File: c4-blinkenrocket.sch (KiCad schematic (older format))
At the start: 12 parts, among them J1 ISP, U1 ATtiny88-AU

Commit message: A first complete Version of the Blinkenrocket
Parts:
- added C3: 470 nF, Capacitor_SMD:C_1206_3216Metric_Pad1.42x1.75mm_HandSolder, symbol Device:C
- added H2, H3: MountingHole, MountingHole:MountingHole_3.2mm_M3_Pad, symbol Mechanical:MountingHole
- added JP1: SJ1-3523N, footprints:Jack_3.5mm_CUI_SJ1-3523N_Horizontal, symbol SJ1-3523N:SJ1-3523N
- added JP3, JP4: Conn_01x04, Connector_PinHeader_2.54mm:PinHeader_1x04_P2.54mm_Vertical, symbol Connector_Generic:Conn_01x04
- added LED1: LED_Matrix_8x8, footprints:LED_KWM-30881XVB_8x8_3mm_3.2x3.2mm, symbol LED_Matrix_8x8:LED_Matrix_8x8
- added R4, R5: 10k, Resistor_SMD:R_1206_3216Metric_Pad1.42x1.75mm_HandSolder, symbol Device:R
- added SW1, SW2: SW_SPST, Button_Switch_THT:SW_PUSH_6mm_H5mm, symbol Switch:SW_SPST
- added U2: 24CW640-I_SN, Package_SO:SOIC-8_3.9x4.9mm_P1.27mm, symbol 24CW640:24CW640-I_SN
- C1, C2: footprint Capacitor_SMD:C_1206_3216Metric -> Capacitor_SMD:C_1206_3216Metric_Pad1.42x1.75mm_HandSolder
- H1: renamed from H?; footprint MountingHole:MountingHole_3.2mm_M3 -> MountingHole:MountingHole_3.2mm_M3_Pad
- R1: footprint Resistor_SMD:R_1206_3216Metric -> Resistor_SMD:R_1206_3216Metric_Pad1.42x1.75mm_HandSolder
- R2: renamed from R3; footprint Resistor_SMD:R_1206_3216Metric -> Resistor_SMD:R_1206_3216Metric_Pad1.42x1.75mm_HandSolder
- R3: renamed from R2; footprint Resistor_SMD:R_1206_3216Metric -> Resistor_SMD:R_1206_3216Metric_Pad1.42x1.75mm_HandSolder
- R6: renamed from R4; footprint Resistor_SMD:R_1206_3216Metric -> Resistor_SMD:R_1206_3216Metric_Pad1.42x1.75mm_HandSolder
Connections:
- net GND: now also C3.1, JP1.1 (S), JP3.4 (Pin_4), JP4.4 (Pin_4), SW1.2 (B), SW2.2 (B), U2.4 (VSS)
- net MISO: now also LED1.1 (ROW5)
- net MOSI: now also LED1.12 (ROW4)
- net VCC: now also C3.2, JP3.1 (Pin_1), JP4.1 (Pin_1), R4.2, R5.2, U2.8 (VCC)
- net C4: now reaches U1.1 (PD3)
- net C4: now also LED1.10 (COL4)
- net C7: now reaches U1.10 (PD6)
- net C7: now also LED1.15 (COL7)
- net C8: now reaches U1.11 (PD7)
- net C8: now also LED1.16 (COL8)
- net R1: now reaches U1.12 (PB0)
- net R1: now also LED1.9 (ROW1)
- net R2: now reaches U1.13 (PB1)
- net R2: now also LED1.14 (ROW2)
- net R3: now reaches U1.14 (PB2)
- net R3: now also LED1.8 (ROW3)
- net C5: now reaches U1.2 (PD4)
- net C5: now also LED1.6 (COL5)
- net B1: now reaches U1.20 (PC7)
- net B1: now also SW1.1 (A)
- net E4: now reaches U1.22 (PA1)
- net E4: now also JP4.3 (Pin_3)
- net E1: now reaches U1.23 (PC0)
- net E1: now also JP3.2 (Pin_2)
- net E2: now reaches U1.24 (PC1)
- net E2: now also JP3.3 (Pin_3)
- net E3: now reaches U1.25 (PC2)
- net E3: now also JP4.2 (Pin_2)
- net B2: now reaches U1.26 (PC3)
- net B2: now also SW2.1 (A)
- net SDA: now reaches U1.27 (PC4)
- net SDA: now also R4.1, U2.5 (SDA)
- net SCL: now reaches U1.28 (PC5)
- net SCL: now also R5.1, U2.6 (SCL)
- net C1: now reaches U1.30 (PD0)
- net C1: now also LED1.13 (COL1)
- net C2: now reaches U1.31 (PD1)
- net C2: now also LED1.3 (COL2)
- net C3: now reaches U1.32 (PD2)
- net C3: now also LED1.4 (COL3)
- net R7: now reaches U1.7 (PB6)
- net R7: now also LED1.2 (ROW7)
- net R8: now reaches U1.8 (PB7)
- net R8: now also LED1.5 (ROW8)
- net C6: now reaches U1.9 (PD5)
- net C6: now also LED1.11 (COL6)
- net at R3.2: now also JP1.3 (R)
- net SCK renamed R6
- net R6: now also LED1.7 (ROW6)
- no-connect marks 0 -> 2
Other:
- moved on the sheet: C1, C2, D1, D2, H1, R1, R2, R3, U1

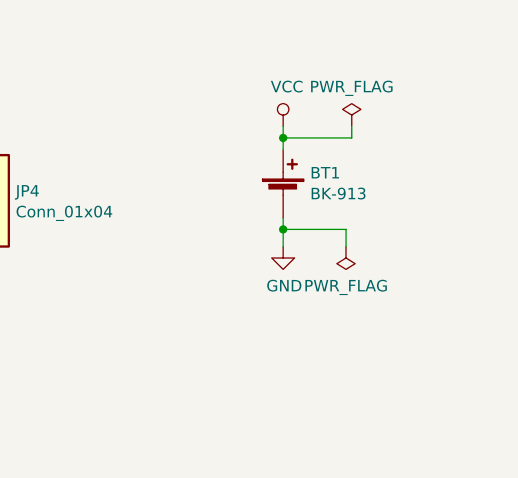
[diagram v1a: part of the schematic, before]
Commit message: Swapped battery holder, made footprints easier to solder
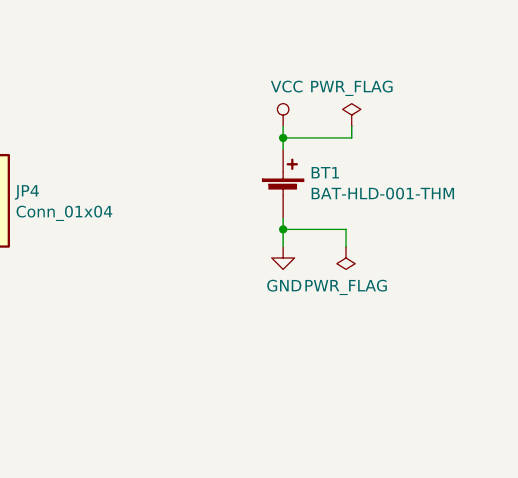
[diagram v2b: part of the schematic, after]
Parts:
- BT1: value BK-913 -> BAT-HLD-001-THM; footprint footprints:BAT_BK-913_footprint -> footprints:BAT_Linx_BAT-HLD-001-THM; Description Battery Retainer Coin, 20.0mm 1 Cell PC Pin -> BATTERY RETAINER COIN PC PIN; Digikey BK-913-ND -> BAT-HLD-001-THM-ND; Mfg Name MPD (Memory Protection Devices) -> Linx Technologies Inc.; Mfg Part Num BK-913 -> BAT-HLD-001-THM
- U1: footprint Package_QFP:TQFP-32_7x7mm_P0.8mm -> footprints:TQFP-32_7x7mm_P0.8mm_Handsolder; Description (none) -> IC MCU 8BIT 8KB FLASH 32TQFP; Digikey (none) -> ATTINY88-AU-ND; Mfg Name (none) -> Microchip Technology; Mfg Part Num (none) -> ATTINY88-AU
- U2: footprint Package_SO:SOIC-8_3.9x4.9mm_P1.27mm -> footprints:SOIC-8_4.9x3.9mm_P1.27mm_Handsolder
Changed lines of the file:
@@
 F 0 "U1" H 1675 1025 50  0000 R CNN
 F 1 "ATtiny88-AU" H 2675 4525 50  0000 R CNN
-F 2 "Package_QFP:TQFP-32_7x7mm_P0.8mm" H 2075 2775 50  0001 C CIN
+F 2 "footprints:TQFP-32_7x7mm_P0.8mm_Handsolder" H 2075 2775 50  0001 C CIN
 F 3 "http://ww1.microchip.com/downloads/en/DeviceDoc/doc8008.pdf" H 2075 2775 50  0001 C CNN
+F 4 "Microchip Technology" H 2075 2775 50  0001 C CNN "Mfg Name"
+F 5 "ATTINY88-AU" H 2075 2775 50  0001 C CNN "Mfg Part Num"
+F 6 "ATTINY88-AU-ND" H 2075 2775 50  0001 C CNN "Digikey"
+F 7 "IC MCU 8BIT 8KB FLASH 32TQFP" H 2075 2775 50  0001 C CNN "Description"
 	1    2075 2775
 	1    0    0    -1
@@
 P 10425 1425
 F 0 "BT1" H 10543 1521 50  0000 L CNN
-F 1 "BK-913" H 10543 1430 50  0000 L CNN
-F 2 "footprints:BAT_BK-913_footprint" V 10425 1485 50  0001 C CNN
-F 3 "http://www.memoryprotectiondevices.com/datasheets/BK-913-datasheet.pdf" V 10425 1485 50  0001 C CNN
-F 4 "MPD (Memory Protection Devices)" H 10425 1425 50  0001 C CNN "Mfg Name"
-F 5 "BK-913 " H 10425 1425 50  0001 C CNN "Mfg Part Num"
-F 6 "BK-913-ND" H 10425 1425 50  0001 C CNN "Digikey"
-F 7 "Battery Retainer Coin, 20.0mm 1 Cell PC Pin " H 10425 1425 50  0001 C CNN "Description"
+F 1 "BAT-HLD-001-THM" H 10543 1430 50  0000 L CNN
+F 2 "footprints:BAT_Linx_BAT-HLD-001-THM" V 10425 1485 50  0001 C CNN
+F 3 "https://linxtechnologies.com/wp/wp-content/uploads/bat-hld-001-thm.pdf" V 10425 1485 50  0001 C CNN
+F 4 "Linx Technologies Inc." H 10425 1425 50  0001 C CNN "Mfg Name"
+F 5 "BAT-HLD-001-THM" H 10425 1425 50  0001 C CNN "Mfg Part Num"
+F 6 "BAT-HLD-001-THM-ND" H 10425 1425 50  0001 C CNN "Digikey"
+F 7 "BATTERY RETAINER COIN PC PIN" H 10425 1425 50  0001 C CNN "Description"
 	1    10425 1425
 	1    0    0    -1
@@
 F 0 "U2" H 8100 3450 50  0000 R CNN
 F 1 "24CW640-I_SN" H 8850 4100 50  0000 R CNN
-F 2 "Package_SO:SOIC-8_3.9x4.9mm_P1.27mm" H 9400 3300 50  0001 C CNN
+F 2 "footprints:SOIC-8_4.9x3.9mm_P1.27mm_Handsolder" H 9400 3300 50  0001 C CNN
 F 3 "http://ww1.microchip.com/downloads/en/DeviceDoc/24CW16X-24CW32X-24CW64X-24CW128X-Data-Sheet-20005772B.pdf" H 8250 3750 50  0001 C CNN
 	1    8250 3750

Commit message: Fabrication data as ordered at the usual chinese pcb manufactures
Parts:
- C1: Description (none) -> CAP CER 10UF 25V X5R 1206; Digikey (none) -> 1276-1075-1-ND; Mfg Name (none) -> Samsung Electro-Mechanics; Mfg Part Num (none) -> CL31A106KAHNNNE
- C2, C3: Description (none) -> CAP CER 0.47UF 50V X7R 1206; Digikey (none) -> 1276-1118-1-ND; Mfg Name (none) -> Samsung Electro-Mechanics; Mfg Part Num (none) -> CL31B474KBHNNNE
- R1: Description (none) -> RES SMD 8.2K OHM 5% 1/4W 1206; Digikey (none) -> 311-8.2KERCT-ND; Mfg Name (none) -> Yageo; Mfg Part Num (none) -> RC1206JR-078K2L
- R2: Description (none) -> RES SMD 6.2K OHM 5% 1/4W 1206; Digikey (none) -> 311-6.2KERCT-ND; Mfg Name (none) -> Yageo; Mfg Part Num (none) -> RC1206JR-076K2L
- R3: Description (none) -> RES SMD 16 OHM 1% 1/4W 1206; Digikey (none) -> 311-16.0FRCT-ND; Mfg Name (none) -> Yageo; Mfg Part Num (none) -> RC1206FR-0716RL
- R4, R5, R6: Description (none) -> RES SMD 10K OHM 5% 1/4W 1206; Digikey (none) -> 311-10KERCT-ND; Mfg Name (none) -> Yageo; Mfg Part Num (none) -> RC1206JR-0710KL
- U2: Description (none) -> IC EEPROM 64K I2C 1MHZ 8SOIC; Digikey (none) -> 24CW640-I/SN-ND; Mfg Name (none) -> Microchip Technology; Mfg Part Num (none) -> 24CW640-I/SN
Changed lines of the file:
@@
 F 2 "Resistor_SMD:R_1206_3216Metric_Pad1.42x1.75mm_HandSolder" V 1955 6500 50  0001 C CNN
 F 3 "~" H 2025 6500 50  0001 C CNN
+F 4 "RES SMD 16 OHM 1% 1/4W 1206" H 0   0   50  0001 C CNN "Description"
+F 5 "311-16.0FRCT-ND" H 0   0   50  0001 C CNN "Digikey"
+F 6 "Yageo" H 0   0   50  0001 C CNN "Mfg Name"
+F 7 "RC1206FR-0716RL" H 0   0   50  0001 C CNN "Mfg Part Num"
 	1    2025 6500
 	0    1    1    0
@@
 F 2 "Resistor_SMD:R_1206_3216Metric_Pad1.42x1.75mm_HandSolder" V 2905 6275 50  0001 C CNN
 F 3 "~" H 2975 6275 50  0001 C CNN
+F 4 "RES SMD 8.2K OHM 5% 1/4W 1206" H 0   0   50  0001 C CNN "Description"
+F 5 "311-8.2KERCT-ND" H 0   0   50  0001 C CNN "Digikey"
+F 6 "Yageo" H 0   0   50  0001 C CNN "Mfg Name"
+F 7 "RC1206JR-078K2L" H 0   0   50  0001 C CNN "Mfg Part Num"
 	1    2975 6275
 	-1   0    0    1
@@
 F 2 "Resistor_SMD:R_1206_3216Metric_Pad1.42x1.75mm_HandSolder" V 2905 6725 50  0001 C CNN
 F 3 "~" H 2975 6725 50  0001 C CNN
+F 4 "RES SMD 6.2K OHM 5% 1/4W 1206" H 0   0   50  0001 C CNN "Description"
+F 5 "311-6.2KERCT-ND" H 0   0   50  0001 C CNN "Digikey"
+F 6 "Yageo" H 0   0   50  0001 C CNN "Mfg Name"
+F 7 "RC1206JR-076K2L" H 0   0   50  0001 C CNN "Mfg Part Num"
 	1    2975 6725
 	-1   0    0    1
@@
 F 2 "Capacitor_SMD:C_1206_3216Metric_Pad1.42x1.75mm_HandSolder" H 2738 6350 50  0001 C CNN
 F 3 "~" H 2700 6500 50  0001 C CNN
+F 4 "CAP CER 10UF 25V X5R 1206" H 0   0   50  0001 C CNN "Description"
+F 5 "1276-1075-1-ND" H 0   0   50  0001 C CNN "Digikey"
+F 6 "Samsung Electro-Mechanics" H 0   0   50  0001 C CNN "Mfg Name"
+F 7 "CL31A106KAHNNNE" H 0   0   50  0001 C CNN "Mfg Part Num"
 	1    2700 6500
 	0    1    1    0
@@
 F 2 "Capacitor_SMD:C_1206_3216Metric_Pad1.42x1.75mm_HandSolder" H 3338 6575 50  0001 C CNN
 F 3 "~" H 3300 6725 50  0001 C CNN
+F 4 "CAP CER 0.47UF 50V X7R 1206" H 0   0   50  0001 C CNN "Description"
+F 5 "1276-1118-1-ND" H 0   0   50  0001 C CNN "Digikey"
+F 6 "Samsung Electro-Mechanics" H 0   0   50  0001 C CNN "Mfg Name"
+F 7 "CL31B474KBHNNNE" H 0   0   50  0001 C CNN "Mfg Part Num"
 	1    3300 6725
 	-1   0    0    1
@@
 F 2 "Resistor_SMD:R_1206_3216Metric_Pad1.42x1.75mm_HandSolder" V 4680 1725 50  0001 C CNN
 F 3 "~" H 4750 1725 50  0001 C CNN
+F 4 "RES SMD 10K OHM 5% 1/4W 1206" H 0   0   50  0001 C CNN "Description"
+F 5 "311-10KERCT-ND" H 0   0   50  0001 C CNN "Digikey"
+F 6 "Yageo" H 0   0   50  0001 C CNN "Mfg Name"
+F 7 "RC1206JR-0710KL" H 0   0   50  0001 C CNN "Mfg Part Num"
 	1    4750 1725
 	0    -1   -1   0
@@
 F 2 "footprints:SOIC-8_4.9x3.9mm_P1.27mm_Handsolder" H 9400 3300 50  0001 C CNN
 F 3 "http://ww1.microchip.com/downloads/en/DeviceDoc/24CW16X-24CW32X-24CW64X-24CW128X-Data-Sheet-20005772B.pdf" H 8250 3750 50  0001 C CNN
+F 4 "IC EEPROM 64K I2C 1MHZ 8SOIC" H 0   0   50  0001 C CNN "Description"
+F 5 "24CW640-I/SN-ND" H 0   0   50  0001 C CNN "Digikey"
+F 6 "Microchip Technology" H 0   0   50  0001 C CNN "Mfg Name"
+F 7 "24CW640-I/SN" H 0   0   50  0001 C CNN "Mfg Part Num"
 	1    8250 3750
 	1    0    0    -1
@@
 F 2 "Resistor_SMD:R_1206_3216Metric_Pad1.42x1.75mm_HandSolder" V 8930 3325 50  0001 C CNN
 F 3 "~" H 9000 3325 50  0001 C CNN
+F 4 "RES SMD 10K OHM 5% 1/4W 1206" H 0   0   50  0001 C CNN "Description"
+F 5 "311-10KERCT-ND" H 0   0   50  0001 C CNN "Digikey"
+F 6 "Yageo" H 0   0   50  0001 C CNN "Mfg Name"
+F 7 "RC1206JR-0710KL" H 0   0   50  0001 C CNN "Mfg Part Num"
 	1    9000 3325
 	-1   0    0    1
@@
 F 2 "Resistor_SMD:R_1206_3216Metric_Pad1.42x1.75mm_HandSolder" V 9205 3325 50  0001 C CNN
 F 3 "~" H 9275 3325 50  0001 C CNN
+F 4 "RES SMD 10K OHM 5% 1/4W 1206" H 0   0   50  0001 C CNN "Description"
+F 5 "311-10KERCT-ND" H 0   0   50  0001 C CNN "Digikey"
+F 6 "Yageo" H 0   0   50  0001 C CNN "Mfg Name"
+F 7 "RC1206JR-0710KL" H 0   0   50  0001 C CNN "Mfg Part Num"
 	1    9275 3325
 	-1   0    0    1
@@
 F 2 "Capacitor_SMD:C_1206_3216Metric_Pad1.42x1.75mm_HandSolder" H 1063 2525 50  0001 C CNN
 F 3 "~" H 1025 2675 50  0001 C CNN
+F 4 "CAP CER 0.47UF 50V X7R 1206" H 0   0   50  0001 C CNN "Description"
+F 5 "1276-1118-1-ND" H 0   0   50  0001 C CNN "Digikey"
+F 6 "Samsung Electro-Mechanics" H 0   0   50  0001 C CNN "Mfg Name"
+F 7 "CL31B474KBHNNNE" H 0   0   50  0001 C CNN "Mfg Part Num"
 	1    1025 2675
 	-1   0    0    1
